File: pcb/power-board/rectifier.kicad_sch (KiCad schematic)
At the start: 6 parts

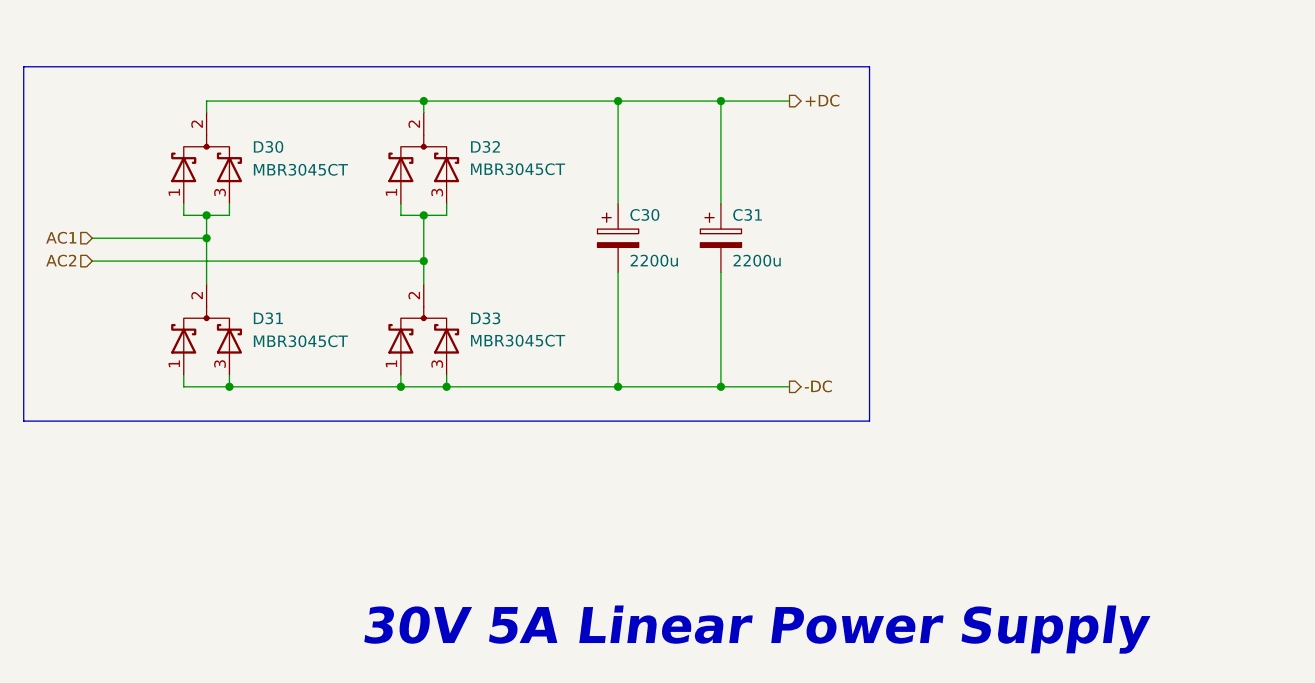
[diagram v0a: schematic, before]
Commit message: Perform minor stylistic changes on power-board schematic, clear DRC
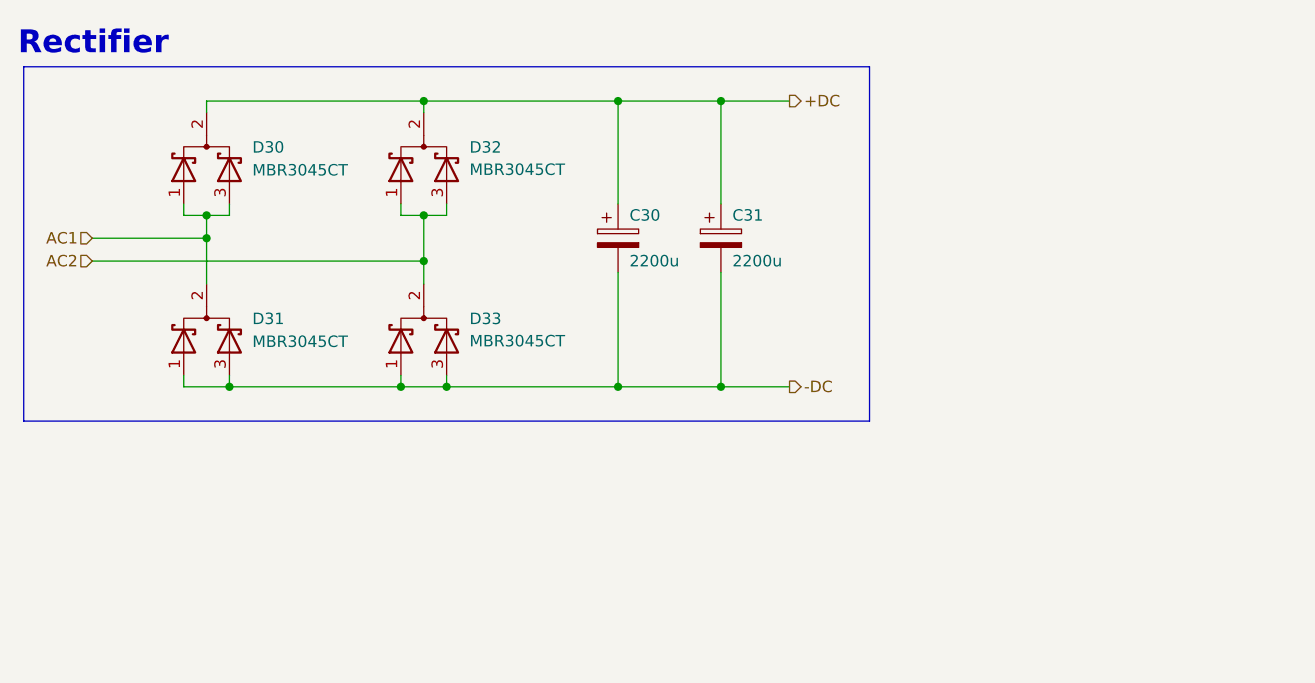
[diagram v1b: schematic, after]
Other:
- note added: "Rectifier"
- note removed: "30V 5A Linear Power Supply"
- title: Rectifier -> DW3005T-power-board
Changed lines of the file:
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@@
 	(paper "A5")
 	(title_block
-		(title "Rectifier")
-		(date "2024-02-24")
-		(rev "V1.0")
+		(title "DW3005T-power-board")
+		(date "2024-02-26")
+		(rev "1.0.0")
 		(company "Dominik Workshop")
 	)
@@
 		)
 	)
-	(text "30V 5A Linear Power Supply"
+	(text "Rectifier"
 		(exclude_from_sim no)
-		(at 95.885 114.3 0)
+		(at 57.785 46.99 0)
 		(effects
 			(font
-				(size 4 4)
-				(thickness 0.8)
+				(size 2.54 2.54)
+				(thickness 0.508)
 				(bold yes)
-				(italic yes)
 			)
-			(justify left bottom)
-		)
-	)
+			(justify left)
+		)
+	)
